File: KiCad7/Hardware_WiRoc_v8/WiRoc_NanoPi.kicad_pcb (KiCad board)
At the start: 4 copper layers, 97.6 x 68.7 mm, 170 parts, among them J1 Conn_02x05_Odd_Even, J10 Conn_01x09_Socket, J2 Conn_01x04, J3 Micro_SD_Card_Det1, J4 Conn_01x09_Socket, J5 Conn_01x04_Socket, J6 HAT_Conn_DBG, J8 Conn_01x06, J9 Conn_Coaxial, SW1 SW_SPST, U1 DRF1268DS, U13 SGM803-RXN3L, U14 KLM8G1WEPD-B031, U2 OLED, U3 AXP209, U4 74LS73, U5 SY6280, U6 BatteryPadM, U7 BatteryPadP, U8 SP3232ECY-L, U9 PCF8563T, Y1 32.768kHz, Y2 24MHz/18pF

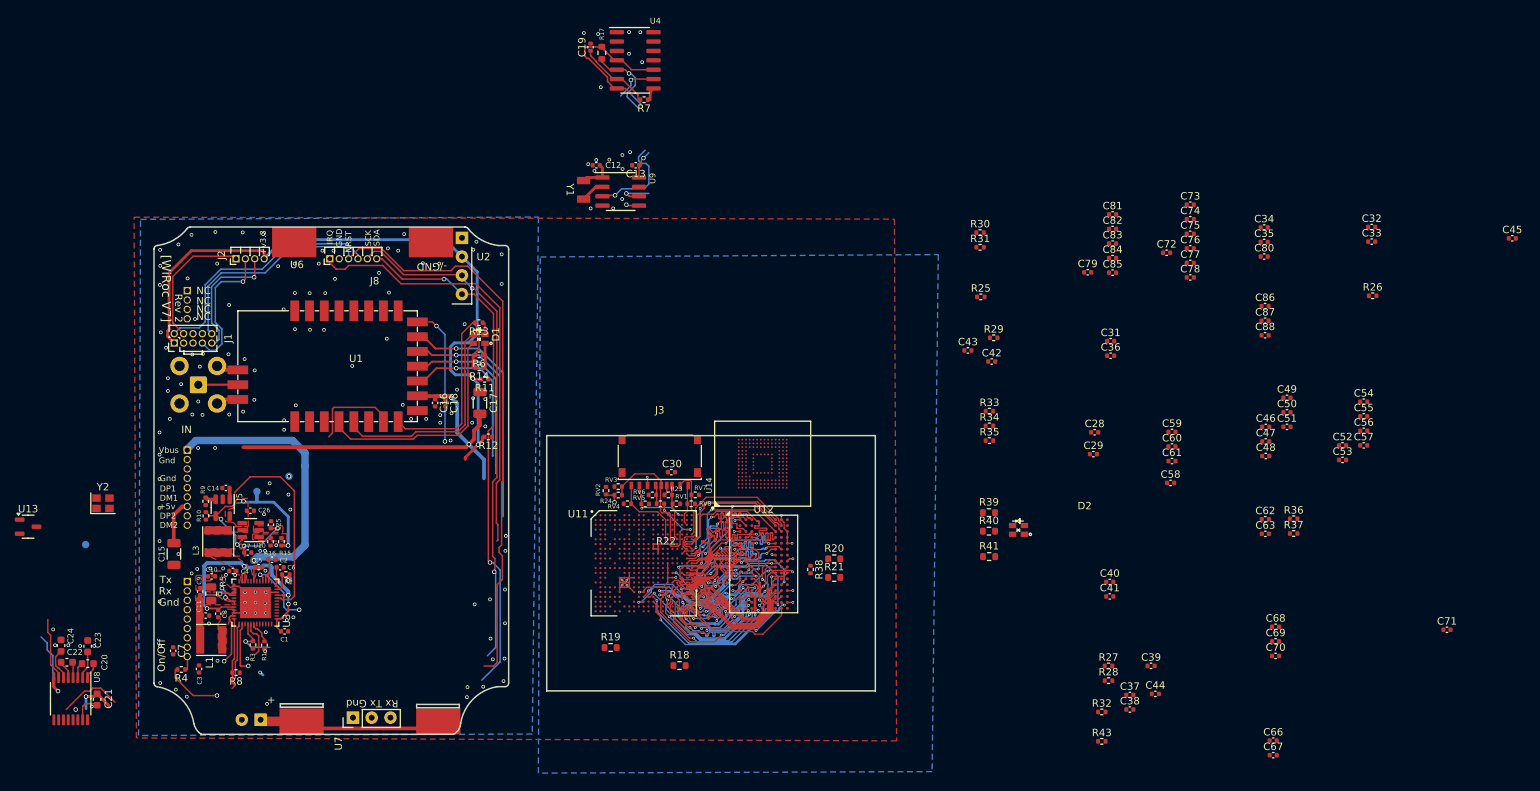
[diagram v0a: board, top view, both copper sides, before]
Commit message: wiroc v8 layout work
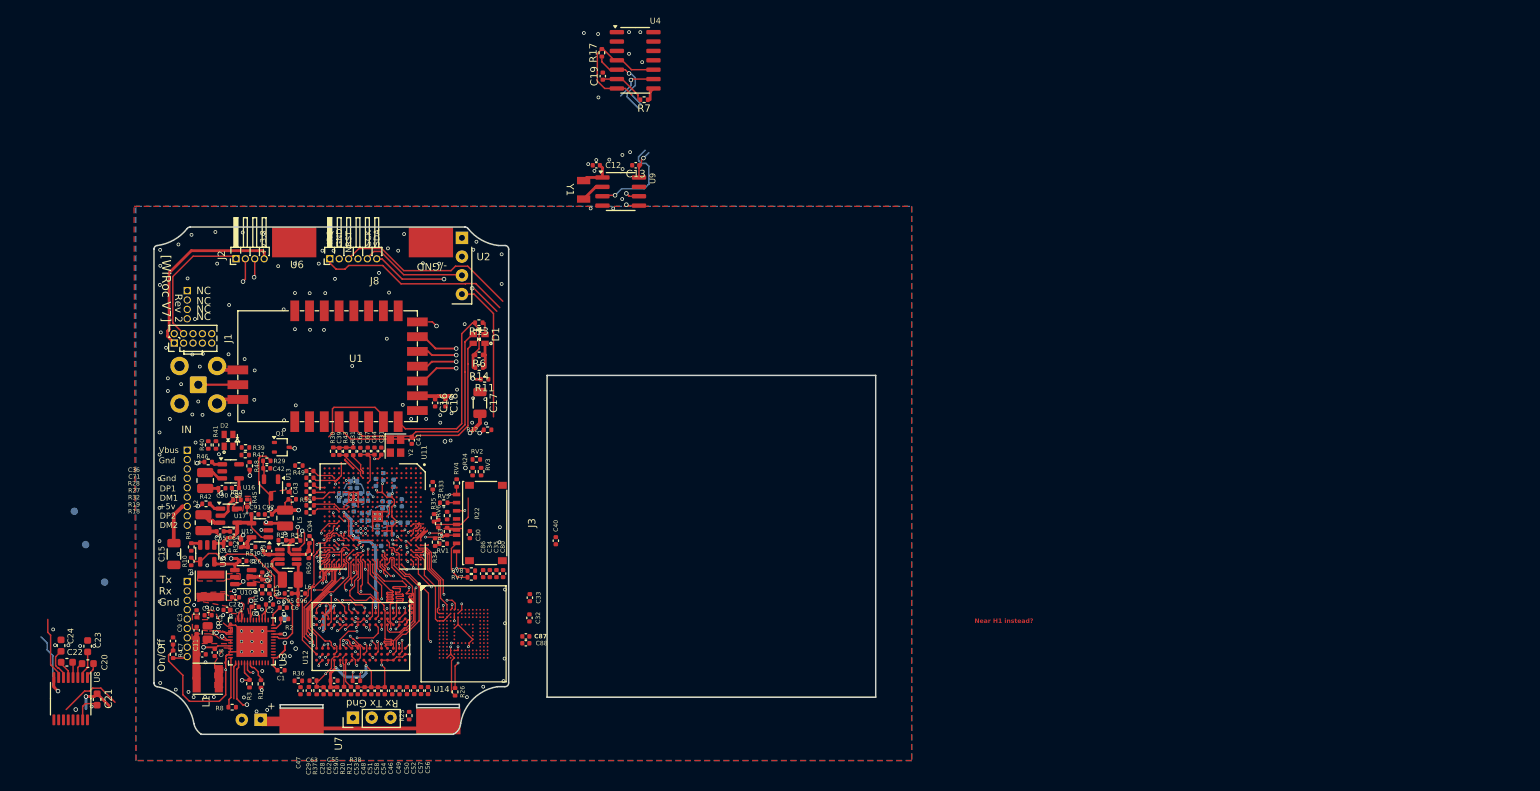
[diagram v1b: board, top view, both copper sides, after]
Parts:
- added C64: 10uF/6.3V, Capacitor_SMD:C_0402_1005Metric, F.Cu at (57.3, 88.0)
- added C65: 10uF, Capacitor_SMD:C_0402_1005Metric, F.Cu at (55.5, 88.0)
- added C89: 10uF/6.3V, Capacitor_SMD:C_0402_1005Metric, F.Cu at (57.5, 82.1)
- added C90: 10uF/6.3V, Capacitor_SMD:C_0402_1005Metric, F.Cu at (55.7, 82.1)
- added C91: 10uF/6.3V, Capacitor_SMD:C_0402_1005Metric, F.Cu at (60.2, 85.7)
- added C92: 10uF/6.3V, Capacitor_SMD:C_0402_1005Metric, F.Cu at (62.0, 85.7)
- added C93: 10uF/6.3V, Capacitor_SMD:C_0402_1005Metric, F.Cu at (62.1, 90.6)
- added C94: 22pF, Capacitor_SMD:C_0402_1005Metric, F.Cu at (67.5, 89.1)
- added C95: 10uF/6.3V, Capacitor_SMD:C_0402_1005Metric, F.Cu at (64.7, 96.4)
- added C96: 10uF/6.3V, Capacitor_SMD:C_0402_1005Metric, F.Cu at (66.5, 96.4)
- added L2: DFE252010P-2R2M=P2, Inductor_SMD:L_1008_2520Metric, F.Cu at (53.2, 86.8)
- added L4: DFE252010P-2R2M=P2, Inductor_SMD:L_1008_2520Metric, F.Cu at (53.4, 81.1)
- added L5: DFE252010P-2R2M=P2, Inductor_SMD:L_1008_2520Metric, F.Cu at (64.2, 86.2)
- added L6: DFE252010P-1R0M=P2, Inductor_SMD:L_1008_2520Metric, F.Cu at (65.0, 94.5)
- added Q1: L2N7002WT1G, Package_TO_SOT_SMD:SOT-323_SC-70, F.Cu at (63.8, 76.6)
- added R42: 10K, Resistor_SMD:R_0402_1005Metric, F.Cu at (53.5, 84.3)
- added R44: 10K/1%, Resistor_SMD:R_0402_1005Metric, F.Cu at (57.7, 83.7)
- added R45: 15K/1%, Resistor_SMD:R_0402_1005Metric, F.Cu at (59.1, 84.2)
- added R46: 10K, Resistor_SMD:R_0402_1005Metric, F.Cu at (53.8, 78.6)
- added R47: 10K/1%, Resistor_SMD:R_0402_1005Metric, F.Cu at (58.9, 77.7)
- added R48: 10K/1%, Resistor_SMD:R_0402_1005Metric, F.Cu at (59.5, 79.1)
- added R49: 2R/1%, Resistor_SMD:R_0402_1005Metric, F.Cu at (66.1, 79.1)
- added R50: 10K/1%, Resistor_SMD:R_0402_1005Metric, F.Cu at (67.5, 91.1)
- added R51: 6.8K/1%, Resistor_SMD:R_0402_1005Metric, F.Cu at (59.7, 90.1)
- added R52: 30K/1%, Resistor_SMD:R_0402_1005Metric, F.Cu at (58.3, 89.6)
- added R53: 12K/1%, Resistor_SMD:R_0402_1005Metric, F.Cu at (63.9, 89.2)
- added R54: 30K/1%, Resistor_SMD:R_0402_1005Metric, F.Cu at (65.8, 89.2)
- added R55: 10K, Resistor_SMD:R_0402_1005Metric, F.Cu at (65.2, 83.6)
- added U15: RT8059, Package_TO_SOT_SMD:TSOT-23-5, F.Cu at (56.6, 85.9)
- added U16: RT8059, Package_TO_SOT_SMD:TSOT-23-5, F.Cu at (56.9, 79.9)
- added U17: RT8059, Package_TO_SOT_SMD:TSOT-23-5, F.Cu at (60.8, 87.8)
- added U18: MP2143DJ, Package_TO_SOT_SMD:TSOT-23-8, F.Cu at (64.7, 91.4)
- C37, C38, C45, C60, C61, C68, C69, C70, C72, C73, C74, C75, C76, C77, C78, C79, C81, C82, C83, C84, C85: moved to B.Cu
- R17, R18, R19, R20, R21, R39, R40, R41: footprint Resistor_SMD:R_0603_1608Metric -> Resistor_SMD:R_0402_1005Metric
- moved C71 155.2 mm to (67.6, 80.7), turned to 180 degrees
- moved C45 155.0 mm to (78.9, 81.5), turned to 90 degrees
- moved C55 143.9 mm to (70.9, 108.2)
- moved C54 138.1 mm to (77.7, 109.6), turned to -90 degrees
- moved C53 136.9 mm to (74.1, 109.6), turned to -90 degrees
- moved R36 136.5 mm to (66.0, 108.2)
- moved R26 135.2 mm to (87.2, 109.7), turned to 90 degrees
- moved C47 134.9 mm to (66.3, 109.6), turned to -90 degrees
- moved R37 133.9 mm to (68.5, 109.5), turned to -90 degrees
- moved C57 131.8 mm to (82.6, 109.5), turned to -90 degrees
- moved C56 131.4 mm to (83.6, 109.5), turned to -90 degrees
- moved C63 130.4 mm to (68.0, 108.2), turned to 180 degrees
- moved C52 129.9 mm to (81.7, 109.5), turned to -90 degrees
- moved C66 129.6 mm to (74.4, 77.2), turned to 90 degrees
- moved C67 129.3 mm to (75.4, 77.1), turned to 90 degrees
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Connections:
- R1 pad 2: N_VBUSEN -> Net-(U3-N_VBUSEN)
- U11 pad B15: SRR_NRST -> WIFI-SPI-CS0
- U11 pad B16: unconnected-(U11B-PC2/NAND_CLE/SPI0_CLK-PadB16) -> WIFI-SPI-SCLK
- U11 pad C15: LORAAUX -> WIFI-SPI-MOSI
- U11 pad C16: N_VBUSEN -> WIFI-SPI-MISO
- U11 pad C3: unconnected-(U11C-PG8/UART1_RTS/PG_EINT8-PadC3) -> LORAAUX
- U11 pad D2: unconnected-(U11C-PG11/PCM1_CLK/PG_EINT11-PadD2) -> WIFI-EN
- U11 pad E3: unconnected-(U11C-PG9/UART1_CTS/PG_EINT9-PadE3) -> SRR_NRST
- U3 pad 6: N_VBUSEN -> Net-(U3-N_VBUSEN)
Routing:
- net VCC-DRAM: track 25.6 -> 130.3 mm, vias 15 -> 21
- net VDD_SYS_3.3V: track 102.9 -> 182.5 mm, vias 4 -> 19
- net SRR_NRST: track 105.6 -> 54.1 mm
- net SCK: track 80.9 -> 33.2 mm, vias 4 -> 3
- net SDA: track 80.0 -> 40.9 mm, vias 3 -> 2
- net VDD1V2-SYS: track 0.00 -> 26.6 mm, vias 0 -> 6
- net eMMC-CMD: track 0.00 -> 26.3 mm, vias 0 -> 3
- net SRR_IRQ: track 58.4 -> 32.3 mm, vias 0 -> 1
- net VBUS: track 39.5 -> 15.9 mm
- net eMMC-RST: track 0.00 -> 20.1 mm, vias 0 -> 2
- net LORAAUX: track 33.1 -> 13.6 mm
- net VDD_5V: track 60.6 -> 42.3 mm, vias 2 -> 4
- net GND: track 16.8 -> 33.4 mm, vias 157 -> 181
- net eMMC-D6: track 0.00 -> 15.6 mm, vias 0 -> 2
- net Net-(Q1-D): track 0.00 -> 14.5 mm, vias 0 -> 2
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- added copper zone on In3.Cu, net GND
- added copper zone on In4.Cu, net GND
- added copper zone on F.Cu, net Net-(U15-FB)
- added copper zone on B.Cu, net VDD-CPUX
- added copper zone on B.Cu, net VDD1V2-SYS
- added copper zone on F.Cu, net VDD_SYS_3.3V
- removed copper zone on F.Cu, net Net-(U10-FB)
- removed copper zone on F.Cu, net Net-(U10-OUT)
- removed copper zone on In2.Cu, net VCC-DRAM
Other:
- board size 97.6 x 68.7 mm -> 97.7 x 68.7 mm
- copper layers 4 -> 6
- board text added: "Near H1 instead?"
- board text removed: "24Mhz xtal"
- board text removed: "Audio"
- board text removed: "CPUS"
- board text removed: "DRAM"
- board text removed: "DRAM bottom side"
- board text removed: "DRAM-1"
- board text removed: "DRAM-2"
- board text removed: "DRAM-svref"
- board text removed: "LED"
- board text removed: "Monitorchip"
- board text removed: "Nand"
- board text removed: "UART0_RX"
- board text removed: "USB-SYS"
- board text removed: "VCC-CPUS"
- board text removed: "VDD-CPUX"
- board text removed: "VDD1V2-SYS"
- board text removed: "VDD_SYS_3.3V-1"
- board text removed: "VDD_SYS_3.3V-2"
- board text removed: "eMMC-1"
- board text removed: "eMMC-2"
- board text removed: "eMMC-vddi"
- board text removed: "sdc1"

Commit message: more routing of v8
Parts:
- added U19: ESP32-C6-Board, WiRoc:ESP32Hosted-C6-Board, F.Cu at (56.3, 102.2)
- U18: footprint Package_TO_SOT_SMD:TSOT-23-8 -> WiRoc:TSOT-23-8-Thinner-Pads
- moved C20 87.6 mm to (124.9, 99.7)
- moved C21 87.6 mm to (126.2, 104.5)
- moved C22 87.6 mm to (122.1, 99.5)
- moved C23 87.6 mm to (124.9, 97.3)
- moved C24 87.6 mm to (121.3, 97.2)
- moved U8 87.6 mm to (122.6, 104.4)
- moved C19 47.7 mm to (91.6, 71.5), turned to 180 degrees
- moved U4 46.6 mm to (90.7, 65.8)
- moved R7 46.1 mm to (93.5, 71.5)
- moved R17 45.2 mm to (86.2, 63.2)
- moved C13 39.7 mm to (89.7, 71.5)
- moved C12 37.8 mm to (87.9, 71.5)
- moved U9 37.8 mm to (90.7, 74.7)
- moved Y1 36.8 mm to (85.8, 73.3)
- moved C40 25.4 mm to (78.5, 77.2)
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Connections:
- U11 pad L18: unconnected-(U11D-PD16/MDC-PadL18) -> WIFI-DataReady
- U11 pad L19: unconnected-(U11D-PD17/MDIO-PadL19) -> WIFI-HandShake
- U14 pad M6: eMMC-CMD -> eMMC-CLK
- U14 pad P2: unconnected-(U14-NC102-PadP2) -> GND
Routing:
- net VDD_SYS_3.3V: track 182.5 -> 298.9 mm, vias 19 -> 29
- net SDA: track 40.9 -> 125.5 mm, vias 2 -> 5
- net SCK: track 33.2 -> 111.1 mm, vias 3 -> 4
- net IRQ: track 6.87 -> 77.2 mm, vias 0 -> 2
- net N_OE: track 13.2 -> 76.3 mm
- net LDO1: track 35.4 -> 82.2 mm, vias 3 -> 5
- net UART0_TX: track 0.00 -> 40.3 mm, vias 0 -> 1
- net USBHost-DP2: track 0.00 -> 39.9 mm, vias 0 -> 1
- net USBHost-DM2: track 0.00 -> 38.6 mm, vias 0 -> 1
- net USBHost-DP1: track 0.00 -> 37.4 mm, vias 0 -> 1
- net USBHost-DM1: track 0.00 -> 37.2 mm, vias 0 -> 1
- net  GPIOA10/STATUS-LED: track 0.00 -> 35.6 mm, vias 0 -> 2
- net Net-(U11D-PA5/UART0_RX/PWM0/PA_EINT5): track 0.00 -> 33.8 mm, vias 0 -> 2
- net GPIOL8/PWR-STB: track 4.75 -> 38.1 mm, vias 1 -> 3
- net VDD_5V: track 42.3 -> 69.6 mm
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- added copper zone on In4.Cu, net VDD_SYS_3.3V
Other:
- board size 97.7 x 68.7 mm -> 48 x 68.7 mm

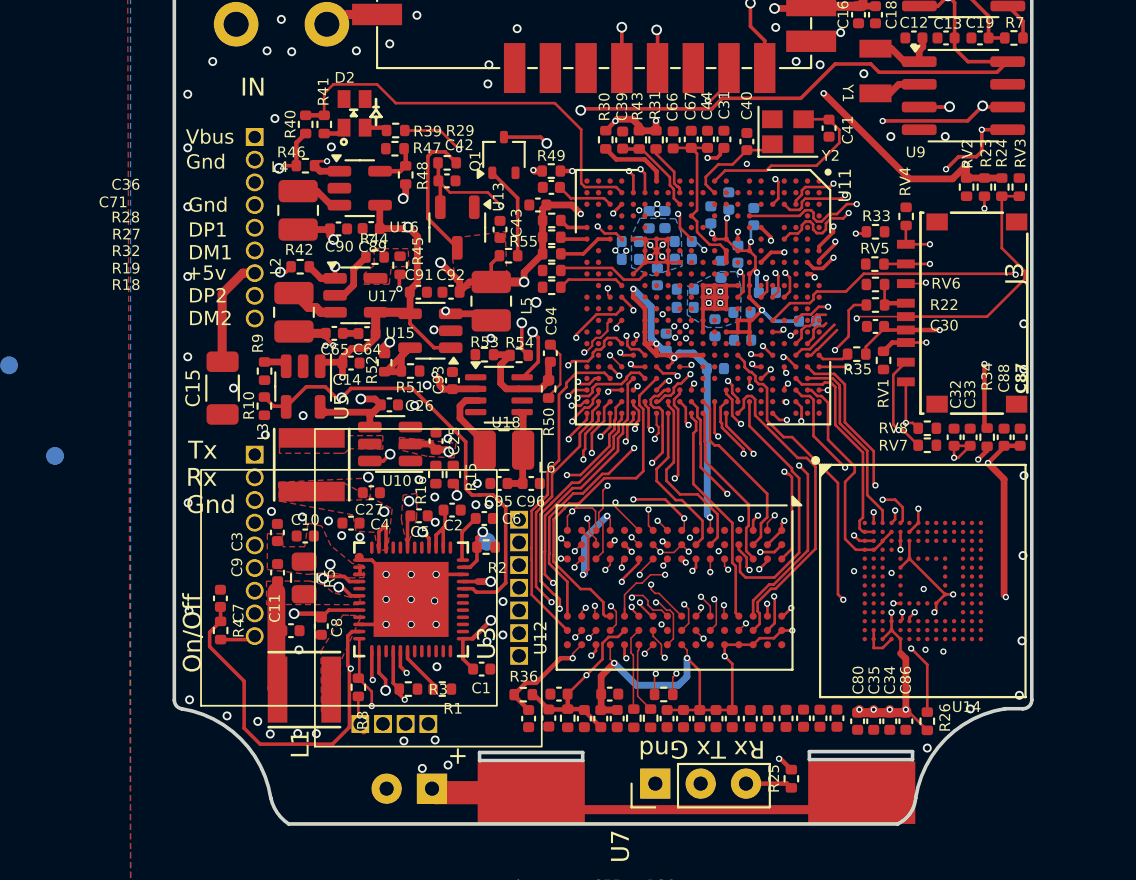
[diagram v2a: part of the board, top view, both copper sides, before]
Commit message: more v8 routing
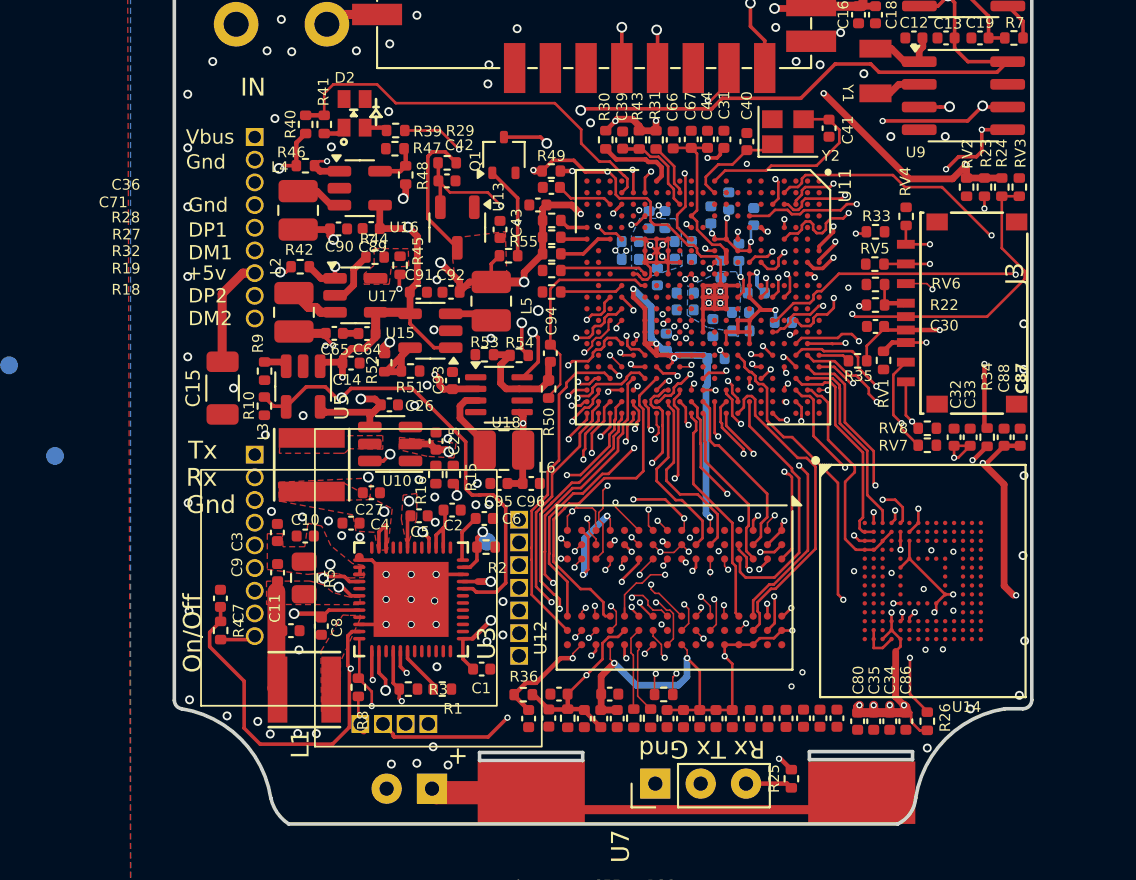
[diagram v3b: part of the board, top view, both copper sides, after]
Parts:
- moved C37 1.36 mm to (80.6, 87.4)
- moved C69 0.63 mm to (79.1, 85.7), turned to 180 degrees
- moved C61 0.57 mm to (76.8, 89.4)
- moved C82 0.52 mm to (78.2, 87.8)
- moved R35 0.38 mm to (84.8, 89.5)
- moved R18 0.26 mm to (67.6, 85.7)
- moved C85 0.21 mm to (75.1, 85.7)
- moved C79 0.14 mm to (75.1, 86.7)
- moved C84 0.12 mm to (76.7, 87.7)
- moved C38 0.11 mm to (78.1, 83.5)
- moved C83 0.08 mm to (78.2, 86.8)
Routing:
- net WIFI-EN: track 0.00 -> 82.0 mm, vias 0 -> 2
- net WIFI-SPI-MISO: track 2.86 -> 54.7 mm, vias 0 -> 1
- net WIFI-SPI-MOSI: track 2.75 -> 53.4 mm, vias 0 -> 1
- net WIFI-SPI-CS0: track 1.79 -> 51.0 mm, vias 0 -> 1
- net WIFI-SPI-SCLK: track 2.24 -> 49.7 mm, vias 0 -> 1
- net WIFI-DataReady: track 0.00 -> 44.9 mm, vias 0 -> 2
- net WIFI-HandShake: track 0.00 -> 44.8 mm, vias 0 -> 2
- net VDD1V2-SYS: track 34.4 -> 63.7 mm, vias 7 -> 8
- net VDD-CPUX: track 18.0 -> 34.8 mm, vias 4 -> 5
- net VDD-CPUFB: track 3.62 -> 12.4 mm
- net GPIOL6/CPUX-VSET: track 5.23 -> 13.0 mm, vias 0 -> 2
- net GND: track 36.2 -> 40.0 mm, vias 167 -> 180
- net SDA: track 125.5 -> 129.1 mm
- net VDD_SYS_3.3V: track 298.9 -> 302.4 mm
- net SCK: track 111.1 -> 114.6 mm
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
